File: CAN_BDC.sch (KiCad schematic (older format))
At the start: 28 parts, among them P1 CONN_01X02, P2 CONN_01X05, P3 CONN_01X02, P4 CONN_01X02, P5 CONN_01X02, P6 CONN_01X01, P7 CONN_01X02, P8 CONN_01X02, P9 CONN_01X01, U1 PSD2CAN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

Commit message: POLOLU_Stepper driver addition
POLOLU_Stepper driver addition
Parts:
- removed C4: 2.2u, Capacitors_SMD:C_0805, symbol C
- removed C5: 0.01u, Capacitors_SMD:C_0402, symbol C
- removed C6: 10u, Capacitors_SMD:c_elec_3x5.3, symbol C
- removed P6, P9: CONN_01X01, Pin_Headers:Pin_Header_Straight_1x01, symbol CONN_01X01
- removed P7, P8: CONN_01X02, Pin_Headers:Pin_Header_Straight_1x02_Pitch2.00mm, symbol CONN_01X02
- removed R3, R4: 0.25, Resistors_SMD:R_2512, symbol R
- removed R6: 10k, Resistors_SMD:R_0402, symbol R
- removed U3: DRV8834, usb_ccb_custom:HTSSOP, symbol DRV8834
- added C4: CP1, Capacitors_SMD:c_elec_3x5.3, symbol CP1
- added P6: CONN_01X02, Pin_Headers:Pin_Header_Straight_1x02_Pitch2.00mm, symbol CONN_01X02
- added P7: CONN_01X04, Pin_Headers:Pin_Header_Straight_1x04, symbol CONN_01X04
- added U3: POLOLU_A4988, usb_ccb_custom:POLOLU_A4988, symbol POLOLU_A4988
- C3: value 0.01u -> 0.22u
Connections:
- net labels added: DRV_MS1, DRV_MS2, DRV_MS3, DRV_nRESET
- net labels removed: DRV_ADECAY, DRV_AOUT1, DRV_AOUT2, DRV_BDECAY, DRV_BOUT1, DRV_BOUT2, DRV_CONFIG, DRV_M0, DRV_M1, DRV_nFAULT
- wire segments 41 -> 27
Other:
- note removed: "MOTOR DRIVE"
- note removed: "OPCJA MICROSTEPING ?\n"
- moved on the sheet: C1, C10, C2, C7, C8, C9, P1, U1, U2, U5

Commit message: buck converter addition
buck converter addition
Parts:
- removed C10, C7: 1u, Capacitors_SMD:C_0402, symbol C
- removed C3: 0.22u, Capacitors_SMD:C_0402, symbol C
- removed U5: MCP1702t, TO_SOT_Packages_SMD:SOT-23, symbol MCP1700T-3302E/TT
- added C5: 470p, Capacitors_SMD:C_0805, symbol CP1
- added C6: 470u, Capacitors_SMD:c_elec_4x5.8, symbol CP1
- added C7: 100n, Capacitors_SMD:c_elec_3x5.3, symbol CP1
- added D1: 1N5819, Resistors_SMD:R_1206, symbol D_Schottky
- added L1: 220uH, Resistors_SMD:R_1210, symbol L_Small
- added L2: 1uH, Resistors_SMD:R_0805, symbol FILTER
- added R1: 2,2k, Resistors_SMD:R_0603, symbol R
- added R2: 0.33, Resistors_SMD:R_0603, symbol R
- added R3: 3,9k, Resistors_SMD:R_0603, symbol R
- added U5: MC33063, usb_ccb_custom:SOIC-8, symbol MC33063
- C4: value CP1 -> 100uF
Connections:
- net +3V3: now also C7.1, L2.2
- net DRV_DIR: now also U4.3 (PF1); no longer U4.10 (PA4)
- net DRV_MS1: now also U4.9 (PA3); no longer U4.3 (PF1)
- net DRV_MS2: now also U4.23 (PA15); no longer U4.26 (PB5)
- net DRV_MS3: now also U4.24 (PB3); no longer U4.25 (PB4)
- net DRV_STEP: now also U4.2 (PF0); no longer U4.9 (PA3)
- net DRV_nENABLE: now also U4.10 (PA4); no longer U4.2 (PF0)
- net DRV_nRESET: now also U4.25 (PB4); no longer U4.24 (PB3)
- net DRV_nSLEEP: now also U4.26 (PB5); no longer U4.23 (PA15)
- net GND: now also C7.2; no longer C4.2, P6.1 (P1), U3.15 (GND), U3.9 (GND)
- net VPP: now also R2.2, U5.6 (Vcc)
- new net: R2.1, U5.1 (SwC), U5.7 (Ipk), U5.8 (DrvC)
- new net: D1.1 (K), L1.1, U5.2 (SwE)
- new net: C5.1, U5.3 (TC)
- new net: R1.1, R3.1, U5.5 (Comp)
- new net: C6.1, L1.2, L2.1, R3.2
- new net GNDA: C4.2, C5.2, C6.2, D1.2 (A), P6.1 (P1), R1.2, U3.15 (GND), U3.9 (GND), U5.4 (GND)
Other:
- moved on the sheet: C4, C8, C9, P6

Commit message: step up converter routing
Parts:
- C4: footprint Capacitors_SMD:c_elec_3x5.3 -> Capacitors_SMD:c_elec_6.3x7.7
- C6: footprint Capacitors_SMD:c_elec_4x5.8 -> Capacitors_SMD:c_elec_8x10
- C7: value 100n -> 100u; footprint Capacitors_SMD:c_elec_3x5.3 -> Capacitors_SMD:c_elec_6.3x5.8
- L1: footprint Resistors_SMD:R_1210 -> usb_ccb_custom:DE0704_Coil
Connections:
- net GNDA is gone; now on net GND: C4.2, C5.2, C6.2, D1.2 (A), P6.1 (P1), R1.2, U3.15 (GND), U3.9 (GND), U5.4 (GND)
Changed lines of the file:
@@
 F 0 "C4" H 9725 5150 50  0000 L CNN
 F 1 "100uF" H 9725 4950 50  0000 L CNN
-F 2 "Capacitors_SMD:c_elec_3x5.3" H 9700 5050 50  0001 C CNN
+F 2 "Capacitors_SMD:c_elec_6.3x7.7" H 9700 5050 50  0001 C CNN
 F 3 "" H 9700 5050 50  0000 C CNN
 	1    9700 5050
@@
 	1    2300 3350
 	1    0    0    -1
-$EndComp
-$Comp
-L GNDA #PWR021
-U 1 1 58093007
-P 2850 3950
-F 0 "#PWR021" H 2850 3700 50  0001 C CNN
-F 1 "GNDA" V 2850 3700 50  0000 C CNN
-F 2 "" H 2850 3950 50  0000 C CNN
-F 3 "" H 2850 3950 50  0000 C CNN
-	1    2850 3950
-	0    -1   -1   0
 $EndComp
 $Comp
@@
 F 0 "C6" H 9100 5950 50  0000 L CNN
 F 1 "470u" H 9100 5850 50  0000 L CNN
-F 2 "Capacitors_SMD:c_elec_4x5.8" H 9000 5900 50  0001 C CNN
+F 2 "Capacitors_SMD:c_elec_8x10" H 9000 5900 50  0001 C CNN
 F 3 "" H 9000 5900 50  0000 C CNN
 	1    9000 5900
@@
 F 0 "L1" V 7000 5000 50  0000 L CNN
 F 1 "220uH" V 6850 4850 50  0000 L CNN
-F 2 "Resistors_SMD:R_1210" H 6900 5050 50  0001 C CNN
+F 2 "usb_ccb_custom:DE0704_Coil" H 6900 5050 50  0001 C CNN
 F 3 "" H 6900 5050 50  0000 C CNN
 	1    6900 5050
@@
 P 9850 5900
 F 0 "C7" H 9950 5950 50  0000 L CNN
-F 1 "100n" H 9950 5850 50  0000 L CNN
-F 2 "Capacitors_SMD:c_elec_3x5.3" H 9850 5900 50  0001 C CNN
+F 1 "100u" H 9950 5850 50  0000 L CNN
+F 2 "Capacitors_SMD:c_elec_6.3x5.8" H 9850 5900 50  0001 C CNN
 F 3 "" H 9850 5900 50  0000 C CNN
 	1    9850 5900
@@
 	6900 4700 9000 4700
 Connection ~ 8400 5250
+$Comp
+L GND #PWR?
+U 1 1 580A6796
+P 2850 3950
+F 0 "#PWR?" H 2850 3700 50  0001 C CNN
+F 1 "GND" H 2858 3777 50  0000 C CNN
+F 2 "" H 2850 3950 50  0000 C CNN
+F 3 "" H 2850 3950 50  0000 C CNN
+	1    2850 3950
+	0    -1   -1   0
+$EndComp
+$Comp
+L GNDA #PWR?
+U 1 1 580A6A98
+P 4150 3550
+F 0 "#PWR?" H 4150 3300 50  0001 C CNN
+F 1 "GNDA" H 4200 3400 50  0000 C CNN
+F 2 "" H 4150 3550 50  0000 C CNN
+F 3 "" H 4150 3550 50  0000 C CNN
+	1    4150 3550
+	1    0    0    -1
+$EndComp
+$Comp
+L GND #PWR?
+U 1 1 580A6AF4
+P 3950 3550
+F 0 "#PWR?" H 3950 3300 50  0001 C CNN
+F 1 "GND" H 3958 3377 50  0000 C CNN
+F 2 "" H 3950 3550 50  0000 C CNN
+F 3 "" H 3950 3550 50  0000 C CNN
+	1    3950 3550
+	1    0    0    -1
+$EndComp
+Wire Wire Line
+	3950 3550 4150 3550
 $EndSCHEMATC

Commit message: Footprints update
Footprints update
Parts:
- added R4: 120, Resistors_SMD:R_0402, symbol R
- C2: value 10u -> 10n
- C4: value 100uF -> 100u
- C6: value 470u -> 330u; footprint Capacitors_SMD:c_elec_8x10 -> Capacitors_SMD:c_elec_6.3x7.7
- C7: footprint Capacitors_SMD:c_elec_6.3x5.8 -> Capacitors_SMD:c_elec_5x5.8
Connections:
- net at P1.2 (P2), U1.1 (C1), U2.6 (CANL): now also R4.2
- net at P1.1 (P1), U1.2 (C2), U2.7 (CANH): now also R4.1
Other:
- moved on the sheet: P1
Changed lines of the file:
@@
 	1    0    0    -1
 $EndComp
-Text Notes 1700 5150 0    118  ~ 0
+Text Notes 1400 4900 0    118  ~ 0
 CAN
 $Comp
@@
 P 4550 5350
 F 0 "C2" H 4350 5350 50  0000 L CNN
-F 1 "10u" H 4400 5250 50  0000 L CNN
+F 1 "10n" H 4400 5250 50  0000 L CNN
 F 2 "Capacitors_SMD:C_0402" H 4588 5200 50  0001 C CNN
 F 3 "" H 4550 5350 50  0000 C CNN
@@
 L CONN_01X02 P1
 U 1 1 57F945E1
-P 1050 5250
-F 0 "P1" H 969 5061 50  0000 C CNN
-F 1 "CONN_01X02" V 924 5106 50  0001 R CNN
-F 2 "Pin_Headers:Pin_Header_Straight_1x02_Pitch2.00mm" H 1050 5250 50  0001 C CNN
-F 3 "" H 1050 5250 50  0000 C CNN
-	1    1050 5250
+P 800 5250
+F 0 "P1" H 719 5061 50  0000 C CNN
+F 1 "CONN_01X02" V 674 5106 50  0001 R CNN
+F 2 "Pin_Headers:Pin_Header_Straight_1x02_Pitch2.00mm" H 800 5250 50  0001 C CNN
+F 3 "" H 800 5250 50  0000 C CNN
+	1    800  5250
 	-1   0    0    1
 $EndComp
@@
 Connection ~ 4250 5550
 Wire Wire Line
-	1250 5200 2500 5200
-Wire Wire Line
-	2500 5300 1250 5300
-Wire Wire Line
 	5100 1400 6050 1400
 Wire Wire Line
@@
 P 9700 5050
 F 0 "C4" H 9725 5150 50  0000 L CNN
-F 1 "100uF" H 9725 4950 50  0000 L CNN
+F 1 "100u" H 9725 4950 50  0000 L CNN
 F 2 "Capacitors_SMD:c_elec_6.3x7.7" H 9700 5050 50  0001 C CNN
 F 3 "" H 9700 5050 50  0000 C CNN
@@
 $EndComp
 $Comp
-L GNDA #PWR022
+L GNDA #PWR021
 U 1 1 58095023
 P 9700 5200
-F 0 "#PWR022" H 9700 4950 50  0001 C CNN
+F 0 "#PWR021" H 9700 4950 50  0001 C CNN
 F 1 "GNDA" H 9800 5050 50  0000 C CNN
 F 2 "" H 9700 5200 50  0000 C CNN
@@
 $EndComp
 $Comp
-L VPP #PWR023
+L VPP #PWR022
 U 1 1 5809511F
 P 9700 4900
-F 0 "#PWR023" H 9700 4750 50  0001 C CNN
+F 0 "#PWR022" H 9700 4750 50  0001 C CNN
 F 1 "VPP" V 9750 5050 50  0000 C CNN
 F 2 "" H 9700 4900 50  0000 C CNN
@@
 Connection ~ 8400 5150
 $Comp
-L VPP #PWR024
+L VPP #PWR023
 U 1 1 580A2B8E
 P 8700 5000
-F 0 "#PWR024" H 8700 4850 50  0001 C CNN
+F 0 "#PWR023" H 8700 4850 50  0001 C CNN
 F 1 "VPP" H 8718 5173 50  0000 C CNN
 F 2 "" H 8700 5000 50  0000 C CNN
@@
 P 9000 5900
 F 0 "C6" H 9100 5950 50  0000 L CNN
-F 1 "470u" H 9100 5850 50  0000 L CNN
-F 2 "Capacitors_SMD:c_elec_8x10" H 9000 5900 50  0001 C CNN
+F 1 "330u" H 9100 5850 50  0000 L CNN
+F 2 "Capacitors_SMD:c_elec_6.3x7.7" H 9000 5900 50  0001 C CNN
 F 3 "" H 9000 5900 50  0000 C CNN
 	1    9000 5900
@@
 	8900 5750 9150 5750
 $Comp
-L GNDA #PWR025
+L GNDA #PWR024
 U 1 1 580A3786
 P 7200 5650
-F 0 "#PWR025" H 7200 5400 50  0001 C CNN
+F 0 "#PWR024" H 7200 5400 50  0001 C CNN
 F 1 "GNDA" H 7300 5500 50  0000 C CNN
 F 2 "" H 7200 5650 50  0000 C CNN
@@
 $EndComp
 $Comp
-L GNDA #PWR026
+L GNDA #PWR025
 U 1 1 580A3846
 P 8450 6050
-F 0 "#PWR026" H 8450 5800 50  0001 C CNN
+F 0 "#PWR025" H 8450 5800 50  0001 C CNN
 F 1 "GNDA" H 8550 5900 50  0000 C CNN
 F 2 "" H 8450 6050 50  0000 C CNN
@@
 $EndComp
 $Comp
-L GNDA #PWR027
+L GNDA #PWR026
 U 1 1 580A3906
 P 9000 6050
-F 0 "#PWR027" H 9000 5800 50  0001 C CNN
+F 0 "#PWR026" H 9000 5800 50  0001 C CNN
 F 1 "GNDA" H 9100 5900 50  0000 C CNN
 F 2 "" H 9000 6050 50  0000 C CNN
@@
 F 0 "C7" H 9950 5950 50  0000 L CNN
 F 1 "100u" H 9950 5850 50  0000 L CNN
-F 2 "Capacitors_SMD:c_elec_6.3x5.8" H 9850 5900 50  0001 C CNN
+F 2 "Capacitors_SMD:c_elec_5x5.8" H 9850 5900 50  0001 C CNN
 F 3 "" H 9850 5900 50  0000 C CNN
 	1    9850 5900
@@
 Connection ~ 9850 5750
 $Comp
-L GND #PWR028
+L GND #PWR027
 U 1 1 580A4A8C
 P 9850 6050
-F 0 "#PWR028" H 9850 5800 50  0001 C CNN
+F 0 "#PWR027" H 9850 5800 50  0001 C CNN
 F 1 "GND" H 9858 5877 50  0000 C CNN
 F 2 "" H 9850 6050 50  0000 C CNN
@@
 Connection ~ 8400 5250
 $Comp
-L GND #PWR?
+L GND #PWR028
 U 1 1 580A6796
 P 2850 3950
-F 0 "#PWR?" H 2850 3700 50  0001 C CNN
+F 0 "#PWR028" H 2850 3700 50  0001 C CNN
 F 1 "GND" H 2858 3777 50  0000 C CNN
 F 2 "" H 2850 3950 50  0000 C CNN
@@
 $EndComp
 $Comp
-L GNDA #PWR?
+L GNDA #PWR029
 U 1 1 580A6A98
 P 4150 3550
-F 0 "#PWR?" H 4150 3300 50  0001 C CNN
+F 0 "#PWR029" H 4150 3300 50  0001 C CNN
 F 1 "GNDA" H 4200 3400 50  0000 C CNN
 F 2 "" H 4150 3550 50  0000 C CNN
@@
 $EndComp
 $Comp
-L GND #PWR?
+L GND #PWR030
 U 1 1 580A6AF4
 P 3950 3550
-F 0 "#PWR?" H 3950 3300 50  0001 C CNN
+F 0 "#PWR030" H 3950 3300 50  0001 C CNN
 F 1 "GND" H 3958 3377 50  0000 C CNN
 F 2 "" H 3950 3550 50  0000 C CNN
@@
 Wire Wire Line
 	3950 3550 4150 3550
+$Comp
+L R R4
+U 1 1 580E2D4A
+P 1850 5200
+F 0 "R4" H 1780 5154 50  0000 R CNN
+F 1 "120" H 1780 5245 50  0000 R CNN
+F 2 "Resistors_SMD:R_0402" H 1780 5291 50  0001 R CNN
+F 3 "" H 1850 5200 50  0000 C CNN
+	1    1850 5200
+	-1   0    0    1
+$EndComp
+Wire Wire Line
+	1600 5050 2100 5050
+Wire Wire Line
+	1600 5050 1600 5200
+Wire Wire Line
+	1600 5200 1000 5200
+Wire Wire Line
+	1000 5300 1750 5300
+Wire Wire Line
+	1750 5350 2000 5350
+Wire Wire Line
+	1750 5300 1750 5350
+Wire Wire Line
+	2000 5350 2000 5300
+Wire Wire Line
+	2000 5300 2500 5300
+Connection ~ 1850 5350
+Wire Wire Line
+	2100 5050 2100 5200
+Wire Wire Line
+	2100 5200 2500 5200
+Connection ~ 1850 5050
 $EndSCHEMATC

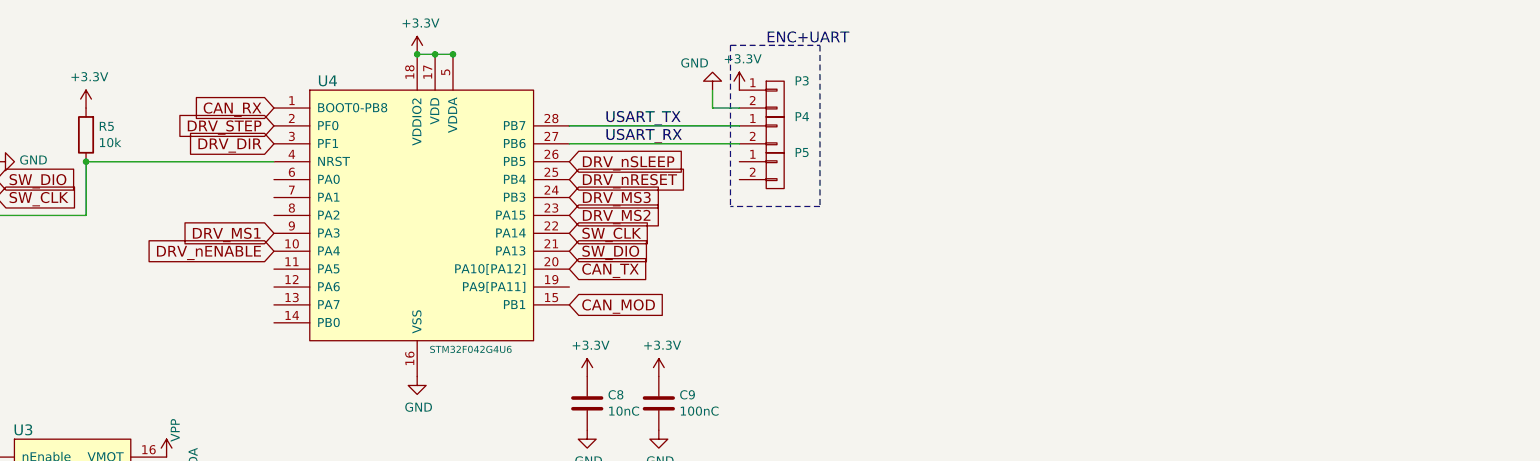
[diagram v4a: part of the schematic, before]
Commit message: Buck Converter Layout update.
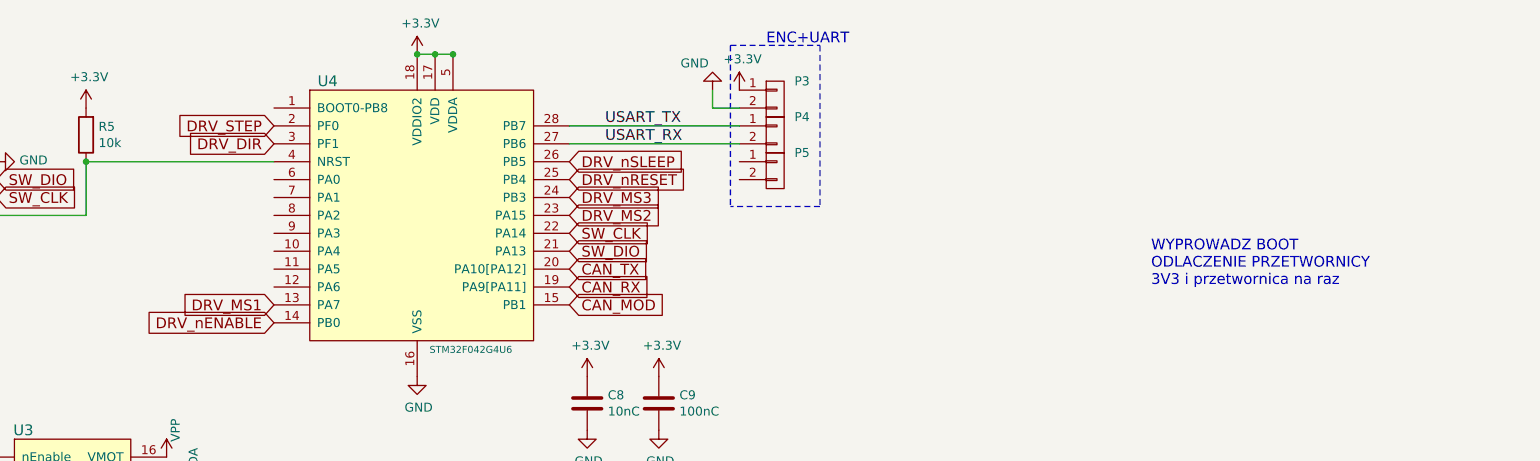
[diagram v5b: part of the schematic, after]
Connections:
- net CAN_RX: now also U4.19 (PA9[PA11]); no longer U4.1 (BOOT0-PB8)
- net DRV_MS1: now also U4.13 (PA7); no longer U4.9 (PA3)
- net DRV_nENABLE: now also U4.14 (PB0); no longer U4.10 (PA4)
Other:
- note added: "WYPROWADZ BOOT\nODLACZENIE PRZETWORNICY\n3V3 i przetwornica na raz\n"
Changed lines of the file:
@@
 Text GLabel 3400 5100 2    60   Input ~ 0
 CAN_RX
-Text GLabel 3450 1300 0    60   Input ~ 0
+Text GLabel 5100 2300 2    60   Input ~ 0
 CAN_RX
 Text GLabel 5100 2400 2    60   Input ~ 0
@@
 	-1   0    0    1
 $EndComp
-Text GLabel 3450 2100 0    60   Input ~ 0
+Text GLabel 3450 2500 0    60   Input ~ 0
 DRV_nENABLE
-Text GLabel 3450 2000 0    60   Input ~ 0
+Text GLabel 3450 2400 0    60   Input ~ 0
 DRV_MS1
 Text GLabel 5100 1900 2    60   Input ~ 0
@@
 	2100 5200 2500 5200
 Connection ~ 1850 5050
+Text Notes 8350 2300 0    60   ~ 0
+WYPROWADZ BOOT\nODLACZENIE PRZETWORNICY\n3V3 i przetwornica na raz\n
 $EndSCHEMATC

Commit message: Layout improve
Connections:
- net DRV_MS1: now also U4.24 (PB3); no longer U4.13 (PA7)
- net DRV_MS2: now also U4.25 (PB4); no longer U4.23 (PA15)
- net DRV_MS3: now also U4.26 (PB5); no longer U4.24 (PB3)
- net DRV_nENABLE: now also U4.23 (PA15); no longer U4.14 (PB0)
- net DRV_nRESET: now also U4.27 (PB6); no longer U4.25 (PB4)
- net DRV_nSLEEP: now also U4.28 (PB7); no longer U4.26 (PB5)
- net GND: now also P2.3 (P3); no longer P2.5 (P5)
- net SW_CLK: now also P2.4 (P4); no longer P2.3 (P3)
- net SW_DIO: now also P2.5 (P5); no longer P2.4 (P4)
- net USART_RX: now also U4.9 (PA3); no longer U4.27 (PB6)
- net USART_TX: now also U4.8 (PA2); no longer U4.28 (PB7)
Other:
- moved on the sheet: P3, P4, P5
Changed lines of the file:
@@
 	1    0    0    -1
 $EndComp
-Text GLabel 1900 1800 2    60   Input ~ 0
+Text GLabel 1900 1700 2    60   Input ~ 0
 SW_CLK
 Text GLabel 5100 2000 2    60   Input ~ 0
 SW_CLK
-Text GLabel 1900 1700 2    60   Input ~ 0
+Text GLabel 1900 1600 2    60   Input ~ 0
 SW_DIO
 Text GLabel 5100 2100 2    60   Input ~ 0
@@
 L GND #PWR011
 U 1 1 571ACD79
-P 5900 1200
-F 0 "#PWR011" H 5900 950 50  0001 C CNN
-F 1 "GND" H 6000 1050 50  0000 C CNN
-F 2 "" H 5900 1200 50  0000 C CNN
-F 3 "" H 5900 1200 50  0000 C CNN
-	1    5900 1200
-	-1   0    0    1
-$EndComp
-Text Label 5300 1400 0    60   ~ 0
-USART_TX
-Text Label 5300 1500 0    60   ~ 0
-USART_RX
+P 1900 2450
+F 0 "#PWR011" H 1900 2200 50  0001 C CNN
+F 1 "GND" H 2000 2300 50  0000 C CNN
+F 2 "" H 1900 2450 50  0000 C CNN
+F 3 "" H 1900 2450 50  0000 C CNN
+	1    1900 2450
+	1    0    0    1
+$EndComp
 $Comp
 L +3.3V #PWR012
@@
 L +3.3V #PWR013
 U 1 1 57F6DF04
-P 6050 1200
-F 0 "#PWR013" H 6050 1050 50  0001 C CNN
-F 1 "+3.3V" H 6068 1373 50  0000 C CNN
-F 2 "" H 6050 1200 50  0000 C CNN
-F 3 "" H 6050 1200 50  0000 C CNN
-	1    6050 1200
-	1    0    0    -1
+P 1750 2450
+F 0 "#PWR013" H 1750 2300 50  0001 C CNN
+F 1 "+3.3V" H 1768 2623 50  0000 C CNN
+F 2 "" H 1750 2450 50  0000 C CNN
+F 3 "" H 1750 2450 50  0000 C CNN
+	1    1750 2450
+	-1   0    0    -1
 $EndComp
 $Comp
@@
 L GND #PWR015
 U 1 1 57056C83
-P 1900 1600
-F 0 "#PWR015" H 1900 1350 50  0001 C CNN
-F 1 "GND" V 1908 1472 50  0000 R CNN
-F 2 "" H 1900 1600 50  0000 C CNN
-F 3 "" H 1900 1600 50  0000 C CNN
-	1    1900 1600
+P 1900 1800
+F 0 "#PWR015" H 1900 1550 50  0001 C CNN
+F 1 "GND" V 1908 1672 50  0000 R CNN
+F 2 "" H 1900 1800 50  0000 C CNN
+F 3 "" H 1900 1800 50  0000 C CNN
+	1    1900 1800
 	0    -1   -1   0
 $EndComp
@@
 L CONN_01X02 P3
 U 1 1 57FD66CE
-P 6250 1250
-F 0 "P3" H 6400 1350 50  0000 C CNN
-F 1 "CONN_01X02" V 6124 1106 50  0001 R CNN
-F 2 "Pin_Headers:Pin_Header_Straight_1x02_Pitch2.00mm" H 6250 1250 50  0001 C CNN
-F 3 "" H 6250 1250 50  0000 C CNN
-	1    6250 1250
-	1    0    0    -1
+P 1550 2500
+F 0 "P3" H 1700 2600 50  0000 C CNN
+F 1 "CONN_01X02" V 1424 2356 50  0001 R CNN
+F 2 "Pin_Headers:Pin_Header_Straight_1x02_Pitch2.00mm" H 1550 2500 50  0001 C CNN
+F 3 "" H 1550 2500 50  0000 C CNN
+	1    1550 2500
+	-1   0    0    -1
 $EndComp
 $Comp
 L CONN_01X02 P4
 U 1 1 57FD69A3
-P 6250 1450
-F 0 "P4" H 6400 1550 50  0000 C CNN
-F 1 "CONN_01X02" V 6124 1306 50  0001 R CNN
-F 2 "Pin_Headers:Pin_Header_Straight_1x02_Pitch2.00mm" H 6250 1450 50  0001 C CNN
-F 3 "" H 6250 1450 50  0000 C CNN
-	1    6250 1450
-	1    0    0    -1
+P 1550 2700
+F 0 "P4" H 1700 2800 50  0000 C CNN
+F 1 "CONN_01X02" V 1424 2556 50  0001 R CNN
+F 2 "Pin_Headers:Pin_Header_Straight_1x02_Pitch2.00mm" H 1550 2700 50  0001 C CNN
+F 3 "" H 1550 2700 50  0000 C CNN
+	1    1550 2700
+	-1   0    0    -1
 $EndComp
 $Comp
@@
 	3400 5200 4550 5200
 Wire Wire Line
-	5900 1300 6050 1300
-Wire Wire Line
-	5900 1300 5900 1200
+	1900 2550 1750 2550
+Wire Wire Line
+	1900 2550 1900 2450
 Connection ~ 2400 1600
 Wire Wire Line
@@
 L CONN_01X02 P5
 U 1 1 58059EA3
-P 6250 1650
-F 0 "P5" H 6400 1750 50  0000 C CNN
-F 1 "CONN_01X02" V 6124 1506 50  0001 R CNN
-F 2 "Pin_Headers:Pin_Header_Straight_1x02_Pitch2.00mm" H 6250 1650 50  0001 C CNN
-F 3 "" H 6250 1650 50  0000 C CNN
-	1    6250 1650
-	1    0    0    -1
+P 1550 2900
+F 0 "P5" H 1700 3000 50  0000 C CNN
+F 1 "CONN_01X02" V 1424 2756 50  0001 R CNN
+F 2 "Pin_Headers:Pin_Header_Straight_1x02_Pitch2.00mm" H 1550 2900 50  0001 C CNN
+F 3 "" H 1550 2900 50  0000 C CNN
+	1    1550 2900
+	-1   0    0    -1
 $EndComp
 Wire Notes Line
-	6000 950  6000 1850
+	1800 2200 1800 3100
 Wire Notes Line
-	6000 950  6500 950
+	1800 2200 1300 2200
 Wire Notes Line
-	6500 950  6500 1850
+	1300 2200 1300 3100
 Wire Notes Line
-	6500 1850 6000 1850
-Text Notes 6200 950  0    60   ~ 0
+	1300 3100 1800 3100
+Text Notes 1600 2200 2    60   ~ 0
 ENC+UART
 $Comp
@@
 Connection ~ 4250 5550
 Wire Wire Line
-	5100 1400 6050 1400
-Wire Wire Line
-	6050 1500 5100 1500
-Wire Wire Line
 	2400 1600 3450 1600
 $Comp
@@
 	-1   0    0    1
 $EndComp
-Text GLabel 3450 2500 0    60   Input ~ 0
+Text GLabel 5100 1900 2    60   Input ~ 0
 DRV_nENABLE
-Text GLabel 3450 2400 0    60   Input ~ 0
+Text GLabel 5100 1800 2    60   Input ~ 0
 DRV_MS1
-Text GLabel 5100 1900 2    60   Input ~ 0
+Text GLabel 5100 1700 2    60   Input ~ 0
 DRV_MS2
-Text GLabel 5100 1800 2    60   Input ~ 0
+Text GLabel 5100 1600 2    60   Input ~ 0
 DRV_MS3
-Text GLabel 5100 1700 2    60   Input ~ 0
+Text GLabel 5100 1500 2    60   Input ~ 0
 DRV_nRESET
-Text GLabel 5100 1600 2    60   Input ~ 0
+Text GLabel 5100 1400 2    60   Input ~ 0
 DRV_nSLEEP
 Text GLabel 3450 1400 0    60   Input ~ 0
@@
 Text Notes 8350 2300 0    60   ~ 0
 WYPROWADZ BOOT\nODLACZENIE PRZETWORNICY\n3V3 i przetwornica na raz\n
+Text Label 3100 2000 0    60   ~ 0
+USART_RX
+Text Label 3100 1900 0    60   ~ 0
+USART_TX
+Wire Wire Line
+	3450 2000 2650 2000
+Wire Wire Line
+	2650 2000 2650 2750
+Wire Wire Line
+	2650 2750 1750 2750
+Wire Wire Line
+	3450 1900 2550 1900
+Wire Wire Line
+	2550 1900 2550 2650
+Wire Wire Line
+	2550 2650 1750 2650
 $EndSCHEMATC
